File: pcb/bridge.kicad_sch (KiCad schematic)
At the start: 46 parts, among them Q4 IRFR4105, Q5 BC817, Q6 IRFR4105, Q7 BC817, Q8 IRFR4105, Q9 IRFR4105, U1 74HC04, U10 LM75B, U2 74HC04

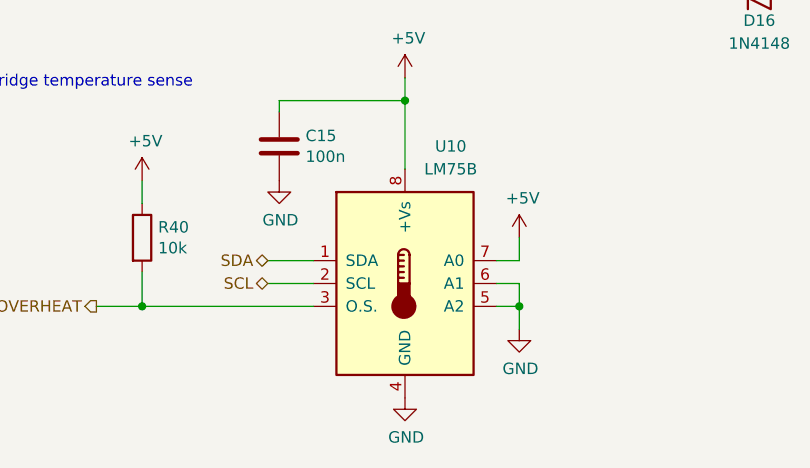
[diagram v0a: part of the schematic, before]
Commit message: Update to KiCad 8.
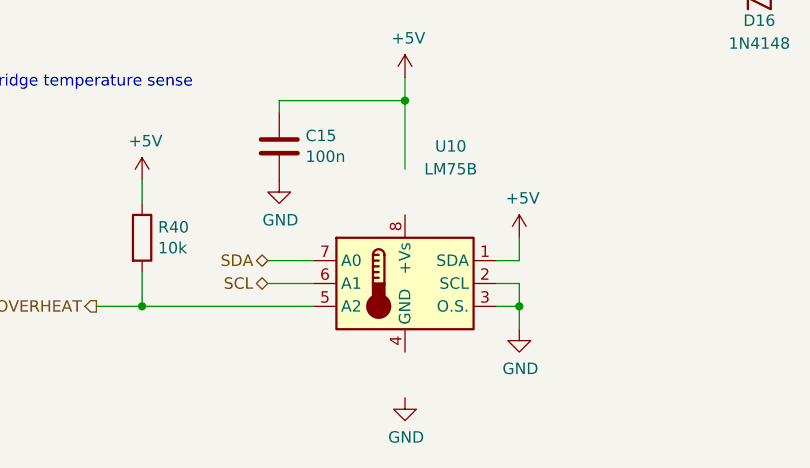
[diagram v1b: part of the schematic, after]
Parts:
- C9: symbol Device:CP -> Device:C_Polarized
- D12, D13: footprint Diode_SMD:D_SOT-23_ANK -> Package_TO_SOT_SMD:SOT-23
- Q5, Q7: footprint Package_TO_SOT_SMD:SOT-23_Handsoldering -> Package_TO_SOT_SMD:SOT-23
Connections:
- net +5V: now also U10.1 (SDA); no longer U10.7 (A0), U10.8 (+Vs)
- net GND: now also U10.2 (SCL), U10.3 (O.S.); no longer U10.4 (GND), U10.5 (A2), U10.6 (A1)
- net J: now also D12.1 (A); no longer D12.2 (A)
- net K: now also D13.1 (A); no longer D13.2 (A)
- net OVERHEAT: now also U10.5 (A2); no longer U10.3 (O.S.)
- net SCL: now also U10.6 (A1); no longer U10.2 (SCL)
- net SDA: now also U10.7 (A0); no longer U10.1 (SDA)
- net U1+: now also D12.3 (K); no longer D12.1 (K)
- net U2+: now also D13.3 (K); no longer D13.1 (K)

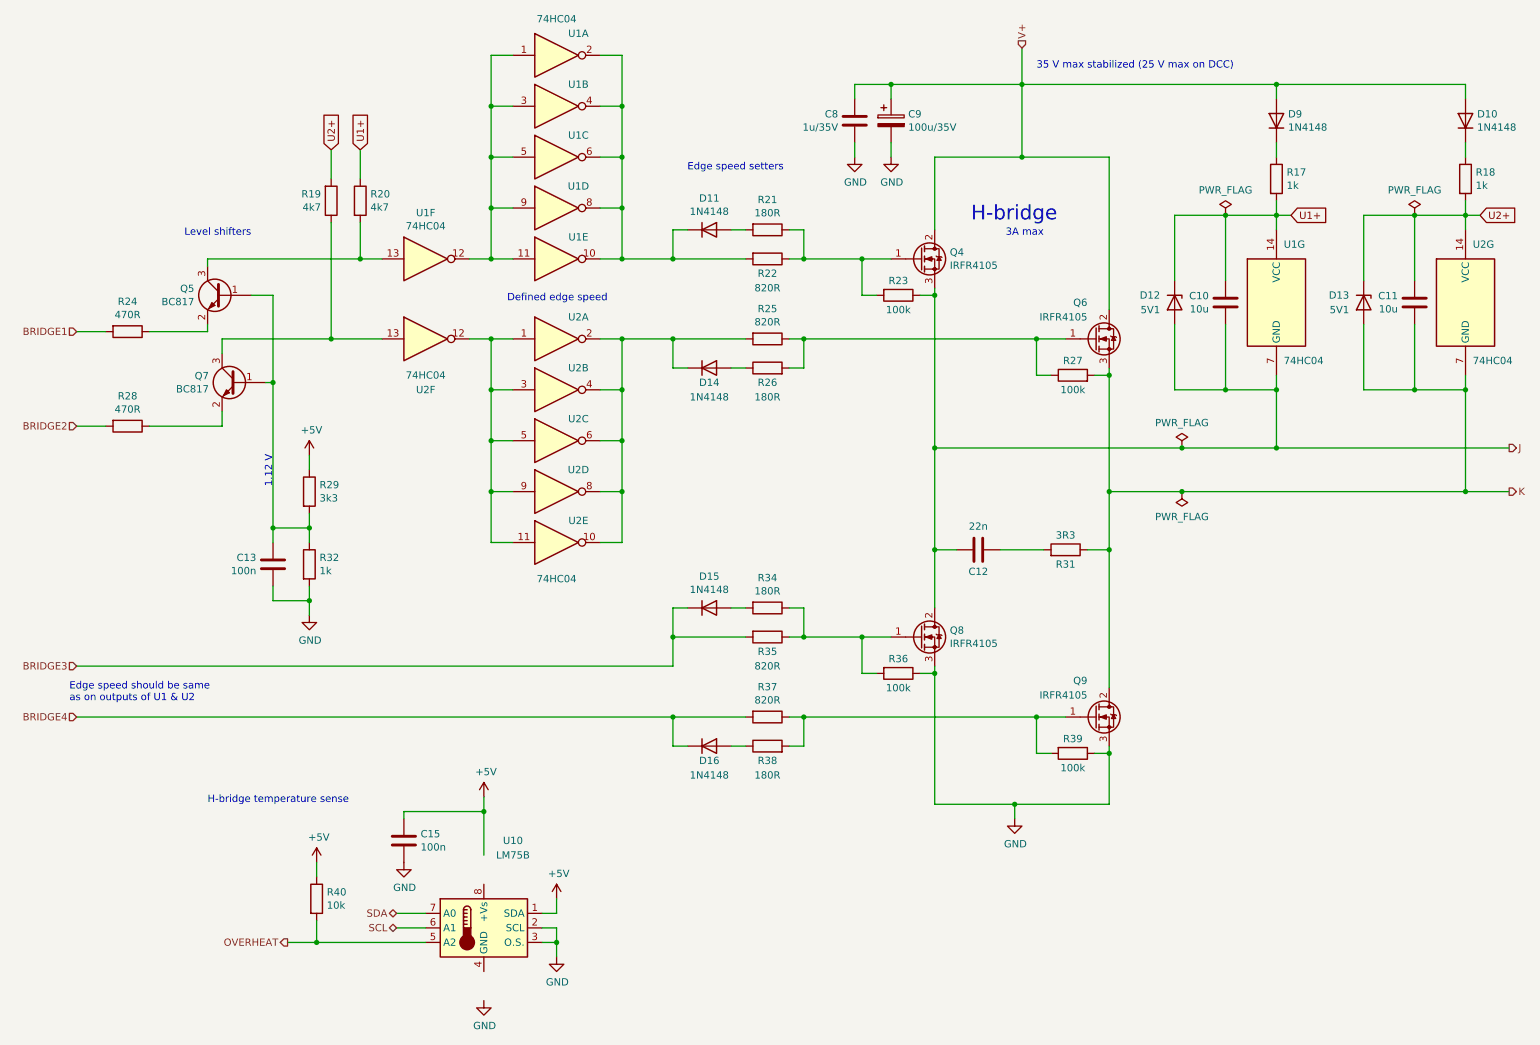
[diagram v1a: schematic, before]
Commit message: Use 1N5819 instead of 1N4148.
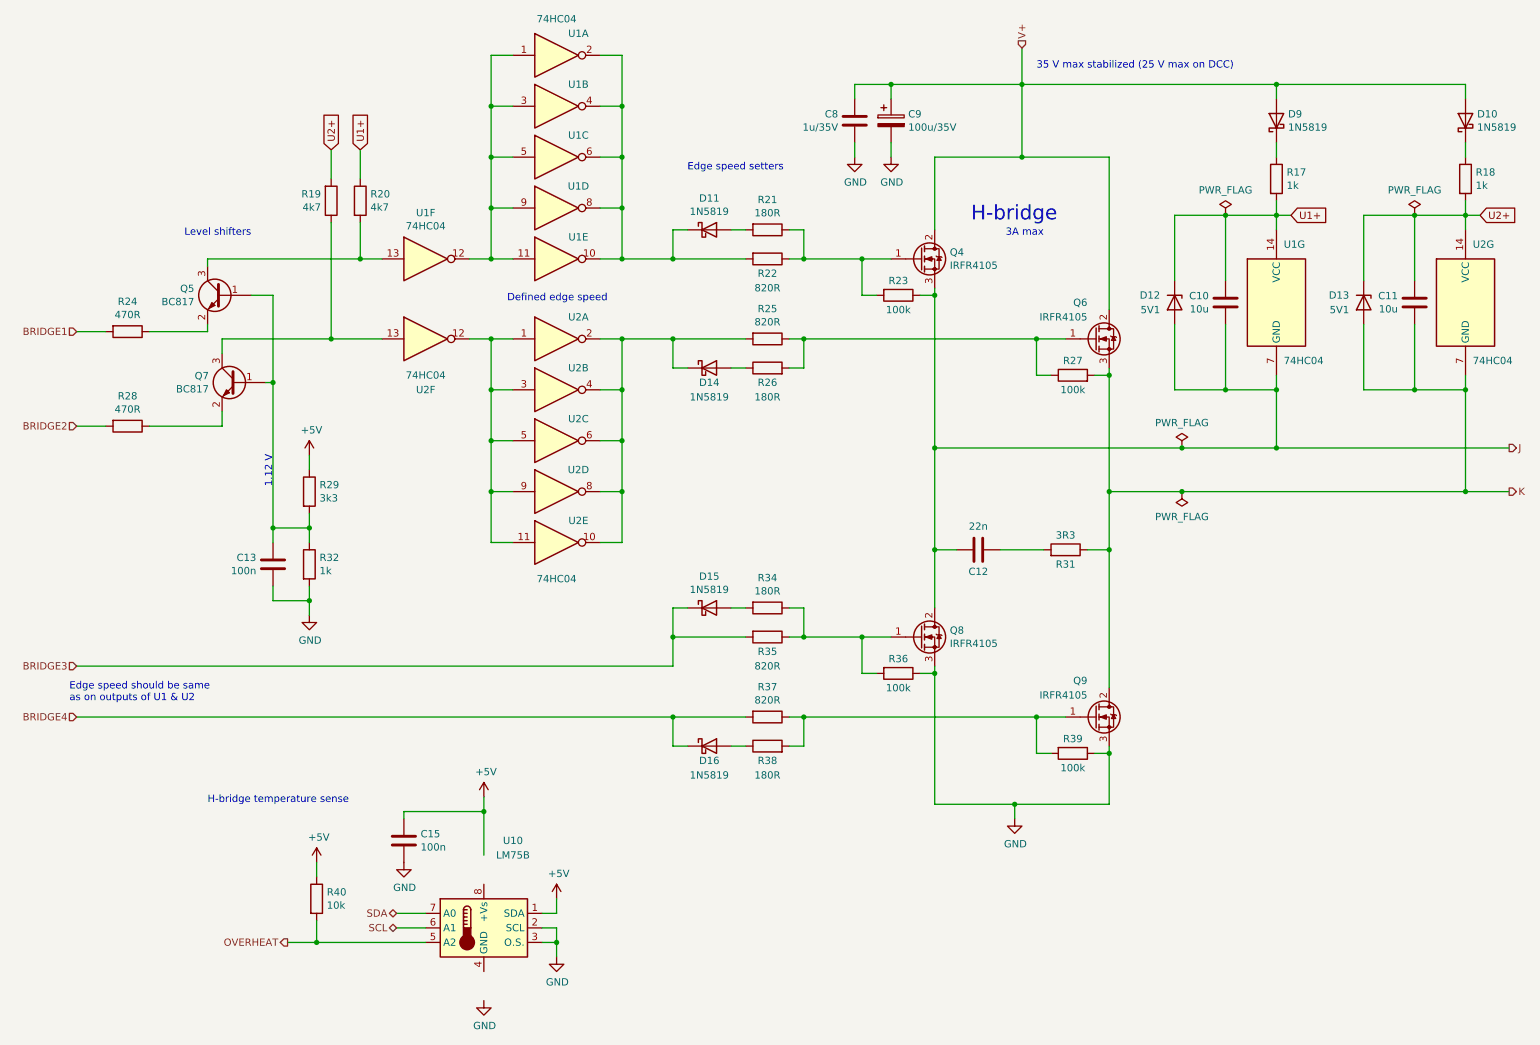
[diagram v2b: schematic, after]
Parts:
- D10, D11, D14, D15, D16, D9: value 1N4148 -> 1N5819; footprint Diode_SMD:D_0805_2012Metric_Pad1.15x1.40mm_HandSolder -> Diode_SMD:D_SOD-123; symbol Device:D -> Device:D_Schottky
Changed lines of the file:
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@@
 	)
 	(symbol
-		(lib_id "Device:D")
+		(lib_id "Device:D_Schottky")
 		(at 137.16 77.47 0)
 		(unit 1)
@@
 			)
 		)
-		(property "Value" "1N4148"
+		(property "Value" "1N5819"
 			(at 137.16 82.55 0)
 			(effects
@@
 			)
 		)
-		(property "Footprint" "Diode_SMD:D_0805_2012Metric_Pad1.15x1.40mm_HandSolder"
+		(property "Footprint" "Diode_SMD:D_SOD-123"
 			(at 137.16 77.47 0)
 			(effects
@@
 			)
 		)
-		(property "Description" "Diode"
+		(property "Description" "Schottky diode"
 			(at 137.16 77.47 0)
 			(effects
@@
 	)
 	(symbol
-		(lib_id "Device:D")
+		(lib_id "Device:D_Schottky")
 		(at 137.16 53.34 0)
 		(unit 1)
@@
 			)
 		)
-		(property "Value" "1N4148"
+		(property "Value" "1N5819"
 			(at 137.16 50.1396 0)
 			(effects
@@
 			)
 		)
-		(property "Footprint" "Diode_SMD:D_0805_2012Metric_Pad1.15x1.40mm_HandSolder"
+		(property "Footprint" "Diode_SMD:D_SOD-123"
 			(at 137.16 53.34 0)
 			(effects
@@
 			)
 		)
-		(property "Description" "Diode"
+		(property "Description" "Schottky diode"
 			(at 137.16 53.34 0)
 			(effects
@@
 	)
 	(symbol
-		(lib_id "Device:D")
+		(lib_id "Device:D_Schottky")
 		(at 236.22 34.29 90)
 		(unit 1)
@@
 			)
 		)
-		(property "Value" "1N4148"
+		(property "Value" "1N5819"
 			(at 238.252 35.433 90)
 			(effects
@@
 			)
 		)
-		(property "Footprint" "Diode_SMD:D_0805_2012Metric_Pad1.15x1.40mm_HandSolder"
+		(property "Footprint" "Diode_SMD:D_SOD-123"
 			(at 236.22 34.29 0)
 			(effects
@@
 			)
 		)
-		(property "Description" "Diode"
+		(property "Description" "Schottky diode"
 			(at 236.22 34.29 0)
 			(effects
@@
 	)
 	(symbol
-		(lib_id "Device:D")
+		(lib_id "Device:D_Schottky")
 		(at 269.24 34.29 90)
 		(unit 1)
@@
 			)
 		)
-		(property "Value" "1N4148"
+		(property "Value" "1N5819"
 			(at 271.272 35.433 90)
 			(effects
@@
 			)
 		)
-		(property "Footprint" "Diode_SMD:D_0805_2012Metric_Pad1.15x1.40mm_HandSolder"
+		(property "Footprint" "Diode_SMD:D_SOD-123"
 			(at 269.24 34.29 0)
 			(effects
@@
 			)
 		)
-		(property "Description" "Diode"
+		(property "Description" "Schottky diode"
 			(at 269.24 34.29 0)
 			(effects
@@
 	)
 	(symbol
-		(lib_id "Device:D")
+		(lib_id "Device:D_Schottky")
 		(at 137.16 143.51 0)
 		(unit 1)
@@
 			)
 		)
-		(property "Value" "1N4148"
+		(property "Value" "1N5819"
 			(at 137.16 148.59 0)
 			(effects
@@
 			)
 		)
-		(property "Footprint" "Diode_SMD:D_0805_2012Metric_Pad1.15x1.40mm_HandSolder"
+		(property "Footprint" "Diode_SMD:D_SOD-123"
 			(at 137.16 143.51 0)
 			(effects
@@
 			)
 		)
-		(property "Description" "Diode"
+		(property "Description" "Schottky diode"
 			(at 137.16 143.51 0)
 			(effects
@@
 	)
 	(symbol
-		(lib_id "Device:D")
+		(lib_id "Device:D_Schottky")
 		(at 137.16 119.38 0)
 		(unit 1)
@@
 			)
 		)
-		(property "Value" "1N4148"
+		(property "Value" "1N5819"
 			(at 137.16 116.1796 0)
 			(effects
@@
 			)
 		)
-		(property "Footprint" "Diode_SMD:D_0805_2012Metric_Pad1.15x1.40mm_HandSolder"
+		(property "Footprint" "Diode_SMD:D_SOD-123"
 			(at 137.16 119.38 0)
 			(effects
@@
 			)
 		)
-		(property "Description" "Diode"
+		(property "Description" "Schottky diode"
 			(at 137.16 119.38 0)
 			(effects
